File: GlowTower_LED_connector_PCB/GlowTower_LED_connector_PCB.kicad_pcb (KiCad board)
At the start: 2 copper layers, 44 x 44 mm, 14 parts, among them SW1 TS-1102S-C-A-B, U1 LED strip, U2 LED strip, U3 LED strip, U4 LED strip, U5 SMTSO3015CTJ, U6 SMTSO3015CTJ

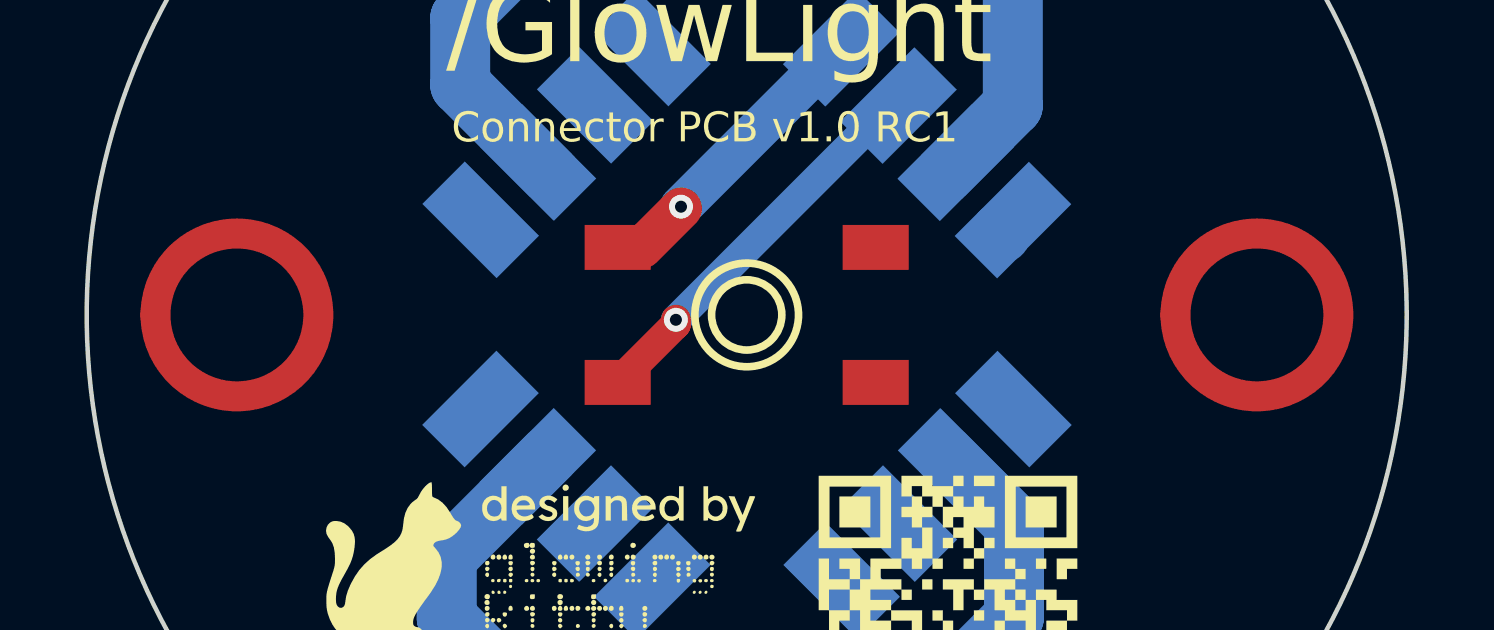
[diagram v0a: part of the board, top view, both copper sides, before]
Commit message: improved connection to top case, added new glowtower design
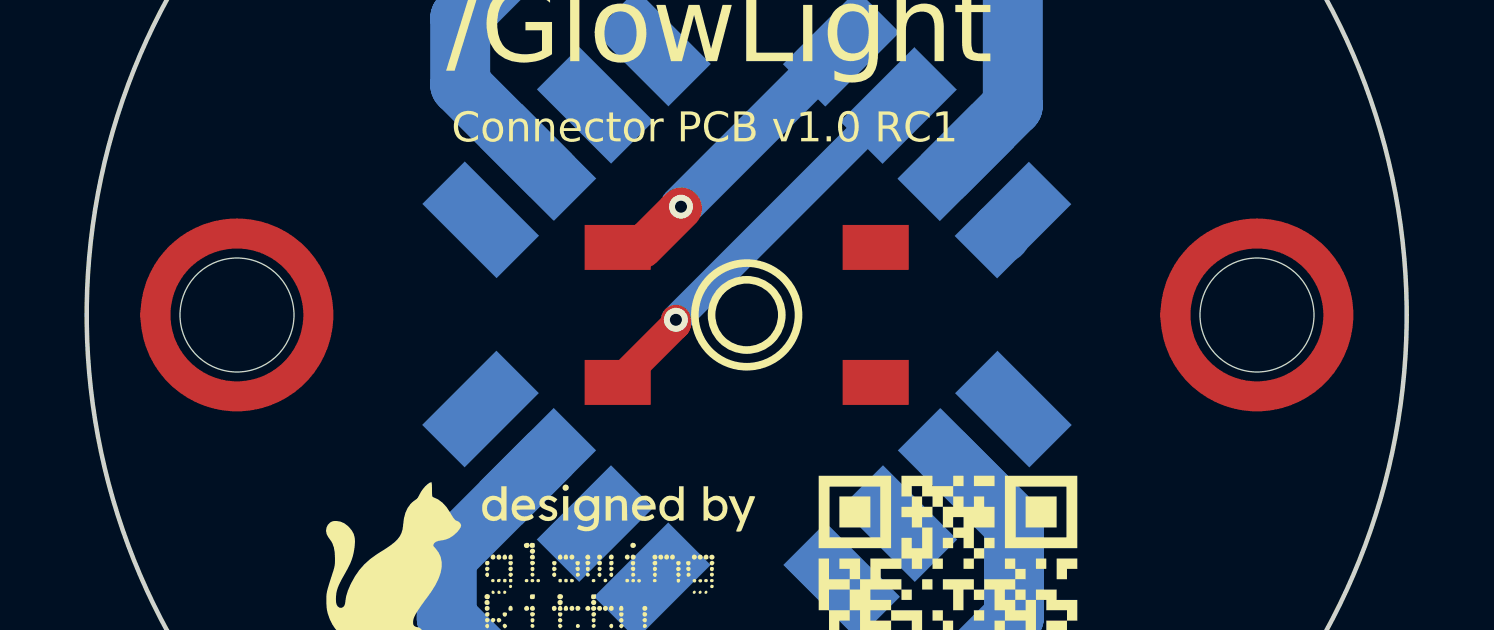
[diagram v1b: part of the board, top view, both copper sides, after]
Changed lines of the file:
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@@
     (property "Sheetfile" "GlowTower_LED_connector_PCB.kicad_sch")
     (property "Sheetname" "")
-    (attr through_hole)
+    (attr through_hole exclude_from_pos_files exclude_from_bom)
     (fp_text reference "U6" (at 0 -4.171704) (layer "F.SilkS") hide
       (effects (font (size 1 1) (thickness 0.15)))
@@
       (effects (font (size 1 1) (thickness 0.15)))
     )
+    (pad "" np_thru_hole circle (at 0.00997 0.00254) (size 3.8 3.8) (drill 3.8) (layers F&B.Cu *.Mask))
     (pad "1" smd custom (at -2.7178 0) (size 1 1) (layers "F.Cu" "F.Paste" "F.Mask")
       (net 17 "unconnected-(U6-Pad1)") (pinfunction "1") (pintype "unspecified")
@@
     (property "Sheetfile" "GlowTower_LED_connector_PCB.kicad_sch")
     (property "Sheetname" "")
-    (attr through_hole)
+    (attr through_hole exclude_from_pos_files exclude_from_bom)
     (fp_text reference "U5" (at 0 -4.171704) (layer "F.SilkS") hide
       (effects (font (size 1 1) (thickness 0.15)))
@@
       (effects (font (size 1 1) (thickness 0.15)))
     )
+    (pad "" np_thru_hole circle (at 0.00997 0.00254) (size 3.8 3.8) (drill 3.8) (layers F&B.Cu *.Mask))
     (pad "1" smd custom (at -2.7178 0) (size 1 1) (layers "F.Cu" "F.Paste" "F.Mask")
       (net 16 "unconnected-(U5-Pad1)") (pinfunction "1") (pintype "unspecified")

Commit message: updated 3D printed parts
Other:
- board text added: "Connector PCB v1.0"
- board text removed: "Connector PCB v1.0 RC1"
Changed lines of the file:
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@@
     (effects (font (size 2.5 2.5) (thickness 0.4)) (justify left))
   )
-  (gr_text "Connector PCB v1.0 RC1" (at 91.76 65.94) (layer "F.SilkS")
+  (gr_text "Connector PCB v1.0" (at 91.76 65.94) (layer "F.SilkS")
     (effects (font (size 1 1) (thickness 0.15)) (justify left))
   )
